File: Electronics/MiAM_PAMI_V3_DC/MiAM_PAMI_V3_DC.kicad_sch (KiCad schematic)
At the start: 28 parts, among them J1 TCRT5000L_Breakout, J2 Conn_01x03_Male, J3 SSD1306_vertical, J4 TCRT5000L_Breakout, J5 TCRT5000L_Breakout, J8 Conn_01x02_Pin, SW1 SW_DPDT_x2, U1 ESP32-DEVKITC-32U, U2 5V, U3 MT3608, U4 5V, U6 TB6612FNG

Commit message: Fix PCB
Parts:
- removed D2: D_Schottky, Diode_SMD:D_SOD-323_HandSoldering, symbol Device:D_Schottky
- U2: value 5V -> 3V3
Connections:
- net 5V_BOARD is gone; now on net +3V3: U2.1 (VO+)
- net +12V: now also U4.3 (IN+)
- net BATTERY_INPUT: now also BAT1.2 (Pin_2); no longer BAT1.1 (Pin_1)
- net EMERGENCY_BUTTON: no longer U4.3 (IN+)
- net GND: now also BAT1.1 (Pin_1); no longer BAT1.2 (Pin_2)
- no-connect marks 15 -> 16
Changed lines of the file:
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@@
   (no_connect (at 120.65 116.84))
   (no_connect (at 34.29 163.83))
+  (no_connect (at 34.29 171.45))
   (no_connect (at 72.39 48.26))
   (no_connect (at 29.845 95.25))
@@
     (stroke (width 0) (type default))
   )
-  (wire (pts (xy 31.115 171.45) (xy 34.29 171.45))
-    (stroke (width 0) (type default))
-  )
   (wire (pts (xy 181.61 157.48) (xy 186.69 157.48))
     (stroke (width 0) (type default))
@@
     (effects (font (size 1.27 1.27)) (justify left bottom))
   )
-  (label "5V_BOARD" (at 23.495 171.45 180) (fields_autoplaced)
-    (effects (font (size 1.27 1.27)) (justify right bottom))
-  )
   (label "RX2" (at 74.93 153.67 0) (fields_autoplaced)
     (effects (font (size 1.27 1.27)) (justify left bottom))
@@
     (effects (font (size 1.27 1.27)) (justify left bottom))
   )
-  (label "EMERGENCY_BUTTON" (at 179.07 86.36 0) (fields_autoplaced)
-    (effects (font (size 1.27 1.27)) (justify left bottom))
-  )
   (label "5V_POWER" (at 173.99 72.39 0) (fields_autoplaced)
     (effects (font (size 1.27 1.27)) (justify left bottom))
@@
   )
   (label "3Y" (at 247.65 128.27 0) (fields_autoplaced)
-    (effects (font (size 1.27 1.27)) (justify left bottom))
-  )
-  (label "5V_BOARD" (at 116.205 58.42 0) (fields_autoplaced)
     (effects (font (size 1.27 1.27)) (justify left bottom))
   )
@@
     )
   )
-  (symbol (lib_id "Connector:Conn_01x02_Female") (at 41.275 36.83 0) (unit 1)
-    (in_bom yes) (on_board yes) (dnp no) (fields_autoplaced)
-    (property "Reference" "BAT1" (at 42.545 36.83 0)
+  (symbol (lib_id "Connector:Conn_01x02_Female") (at 41.275 39.37 0) (mirror x) (unit 1)
+    (in_bom yes) (on_board yes) (dnp no)
+    (property "Reference" "BAT1" (at 42.545 39.37 0)
       (effects (font (size 1.27 1.27)) (justify left))
     )
-    (property "Value" "Screw_Terminal_01x02" (at 42.545 39.37 0)
+    (property "Value" "Screw_Terminal_01x02" (at 42.545 36.83 0)
       (effects (font (size 1.27 1.27)) (justify left))
     )
-    (property "Footprint" "Connector_JST:JST_PH_B2B-PH-K_1x02_P2.00mm_Vertical" (at 41.275 36.83 0)
-      (effects (font (size 1.27 1.27)) hide)
-    )
-    (property "Datasheet" "~" (at 41.275 36.83 0)
+    (property "Footprint" "Connector_JST:JST_PH_B2B-PH-K_1x02_P2.00mm_Vertical" (at 41.275 39.37 0)
+      (effects (font (size 1.27 1.27)) hide)
+    )
+    (property "Datasheet" "~" (at 41.275 39.37 0)
       (effects (font (size 1.27 1.27)) hide)
     )
@@
         (path "/25619b26-f8ce-486a-87c9-e743f43b219f"
           (reference "#PWR035") (unit 1)
-        )
-      )
-    )
-  )
-  (symbol (lib_id "Device:D_Schottky") (at 27.305 171.45 180) (unit 1)
-    (in_bom yes) (on_board yes) (dnp no) (fields_autoplaced)
-    (property "Reference" "D2" (at 27.6225 165.1 0)
-      (effects (font (size 1.27 1.27)))
-    )
-    (property "Value" "D_Schottky" (at 27.6225 167.64 0)
-      (effects (font (size 1.27 1.27)))
-    )
-    (property "Footprint" "Diode_SMD:D_SOD-323_HandSoldering" (at 27.305 171.45 0)
-      (effects (font (size 1.27 1.27)) hide)
-    )
-    (property "Datasheet" "~" (at 27.305 171.45 0)
-      (effects (font (size 1.27 1.27)) hide)
-    )
-    (pin "1")
-    (pin "2")
-    (instances
-      (project "MiAM_PAMI_V3_DC"
-        (path "/25619b26-f8ce-486a-87c9-e743f43b219f"
-          (reference "D2") (unit 1)
         )
       )
@@
       (effects (font (size 1.27 1.27)) (justify left))
     )
-    (property "Value" "5V" (at 101.6 63.5 0)
+    (property "Value" "3V3" (at 101.6 63.5 0)
       (effects (font (size 1.27 1.27)) (justify left))
     )
@@
         (path "/25619b26-f8ce-486a-87c9-e743f43b219f"
           (reference "#PWR032") (unit 1)
+        )
+      )
+    )
+  )
+  (symbol (lib_id "power:+3V3") (at 116.205 58.42 0) (unit 1)
+    (in_bom yes) (on_board yes) (dnp no) (fields_autoplaced)
+    (property "Reference" "#PWR031" (at 116.205 62.23 0)
+      (effects (font (size 1.27 1.27)) hide)
+    )
+    (property "Value" "+3V3" (at 116.205 53.34 0)
+      (effects (font (size 1.27 1.27)))
+    )
+    (property "Footprint" "" (at 116.205 58.42 0)
+      (effects (font (size 1.27 1.27)) hide)
+    )
+    (property "Datasheet" "" (at 116.205 58.42 0)
+      (effects (font (size 1.27 1.27)) hide)
+    )
+    (pin "1")
+    (instances
+      (project "MiAM_PAMI_V3_DC"
+        (path "/25619b26-f8ce-486a-87c9-e743f43b219f"
+          (reference "#PWR031") (unit 1)
         )
       )
@@
         )
       )
+    )
+  )
+  (symbol (lib_id "power:+12V") (at 179.07 86.36 0) (unit 1)
+    (in_bom yes) (on_board yes) (dnp no)
+    (property "Reference" "#PWR025" (at 179.07 90.17 0)
+      (effects (font (size 1.27 1.27)) hide)
+    )
+    (property "Value" "+12V" (at 179.07 81.28 0)
+      (effects (font (size 1.27 1.27)))
+    )
+    (property "Footprint" "" (at 179.07 86.36 0)
+      (effects (font (size 1.27 1.27)) hide)
+    )
+    (property "Datasheet" "" (at 179.07 86.36 0)
+      (effects (font (size 1.27 1.27)) hide)
+    )
+    (pin "1")
+    (instances
+      (project "MiAM_PAMI_V3_DC"
+        (path "/25619b26-f8ce-486a-87c9-e743f43b219f"
+          (reference "#PWR025") (unit 1)
+        )
+      )

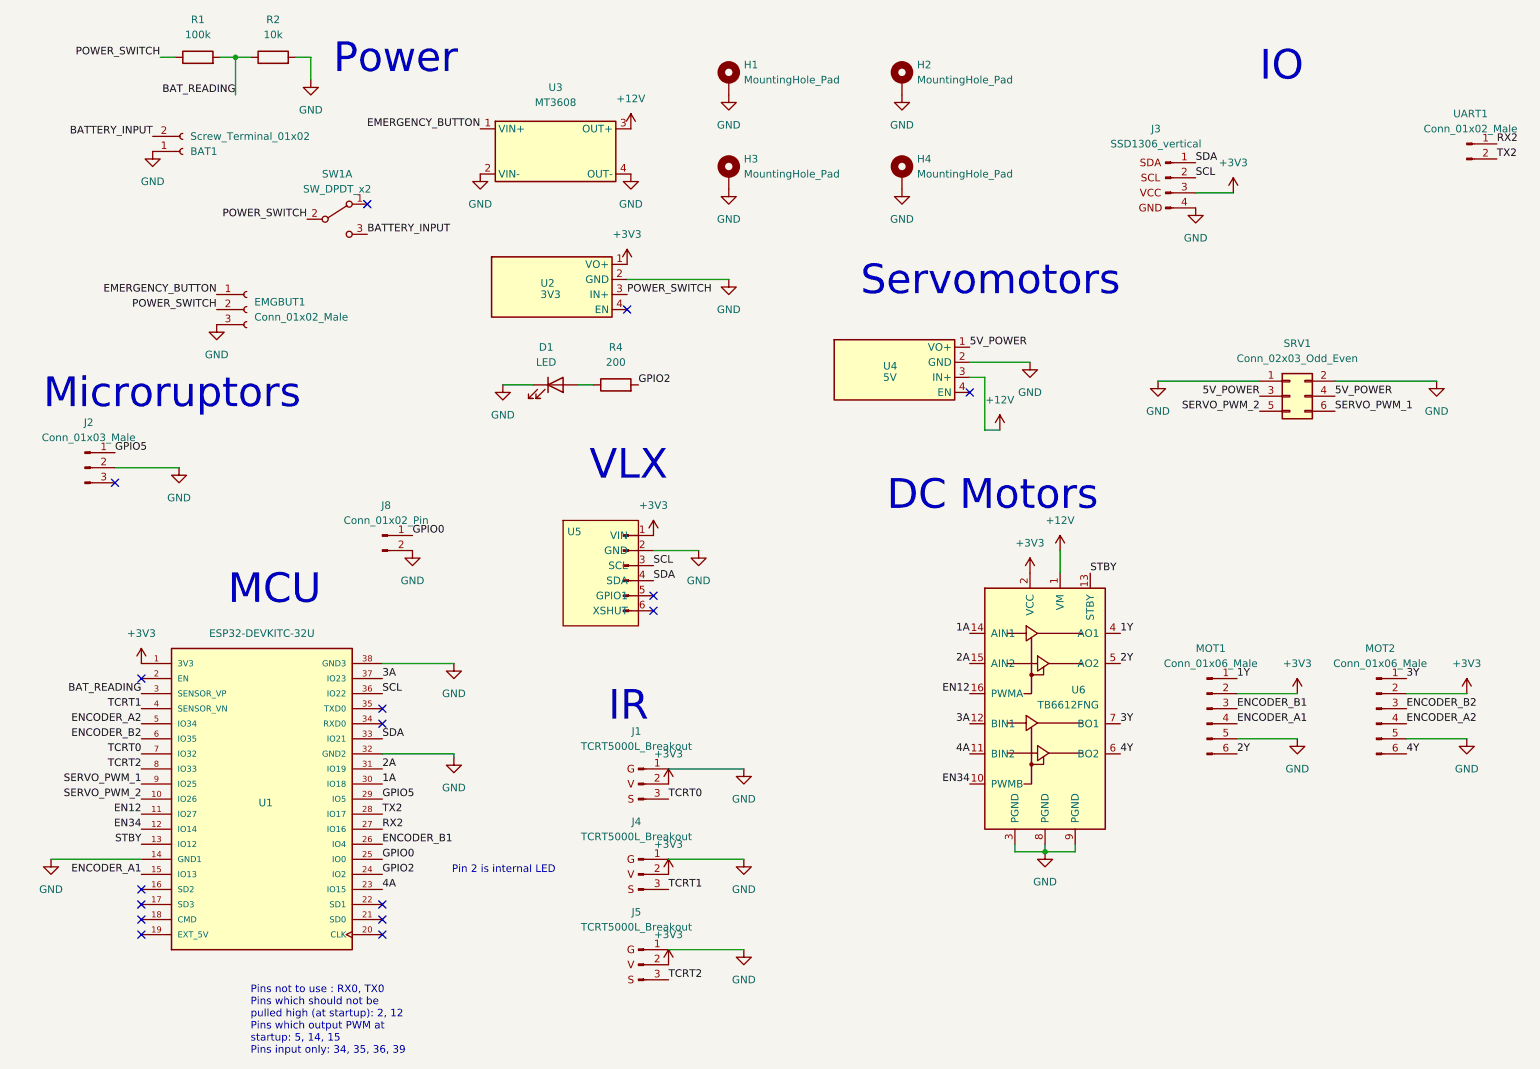
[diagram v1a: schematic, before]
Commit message: Fix DC PAMI schematic
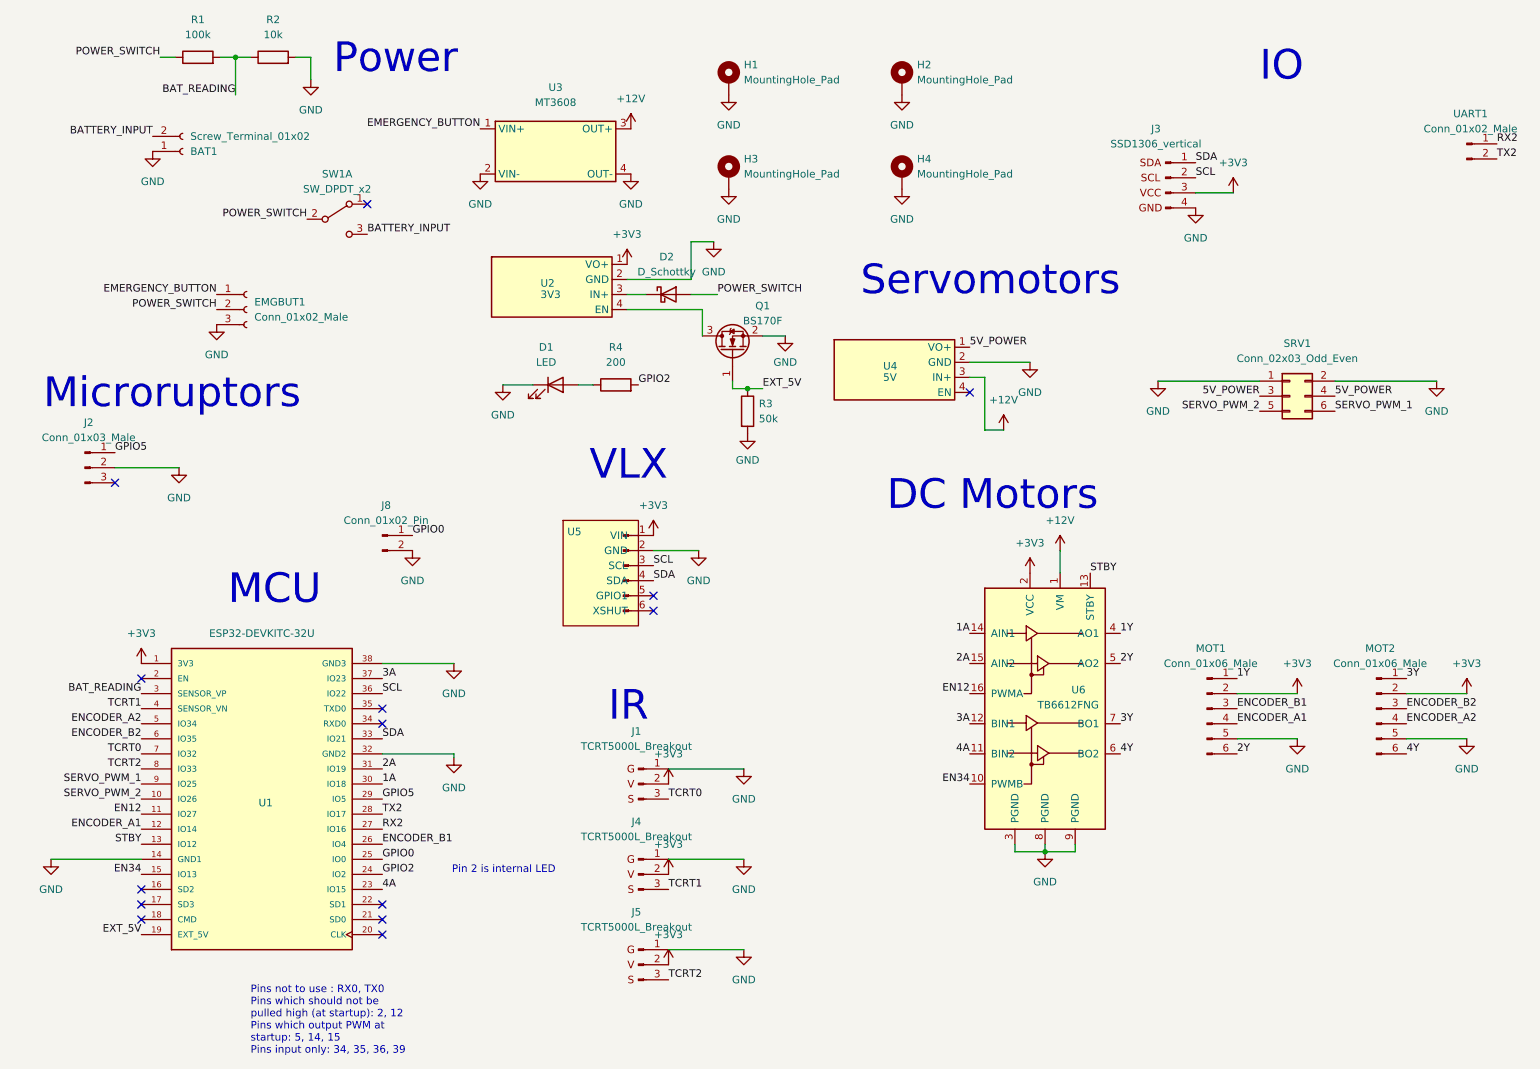
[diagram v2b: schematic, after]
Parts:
- added D2: D_Schottky, Diode_SMD:D_SOD-323_HandSoldering, symbol Device:D_Schottky
- added Q1: BS170F, Package_TO_SOT_SMD:SOT-23, symbol Transistor_FET:BS170F
- added R3: 50k, Resistor_SMD:R_0805_2012Metric, symbol Device:R
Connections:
- net EN34: now also U1.15 (IO13); no longer U1.12 (IO14)
- net ENCODER_A1: now also U1.12 (IO14); no longer U1.15 (IO13)
- net GND: now also Q1.2 (S), R3.2
- net POWER_SWITCH: now also D2.2 (A); no longer U2.3 (IN+)
- net at U2.4 (EN): now also Q1.3 (D)
- net EXT_5V: now reaches U1.19 (EXT_5V)
- net EXT_5V: now also Q1.1 (G), R3.1
- new net: D2.1 (K), U2.3 (IN+)
- no-connect marks 16 -> 14
